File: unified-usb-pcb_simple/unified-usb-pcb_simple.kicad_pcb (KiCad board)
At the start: 2 copper layers, 30 x 34 mm, 12 parts, among them J1 USB_C_Receptacle_USB2.0, J2 USB_Out, U1 SRV05-4

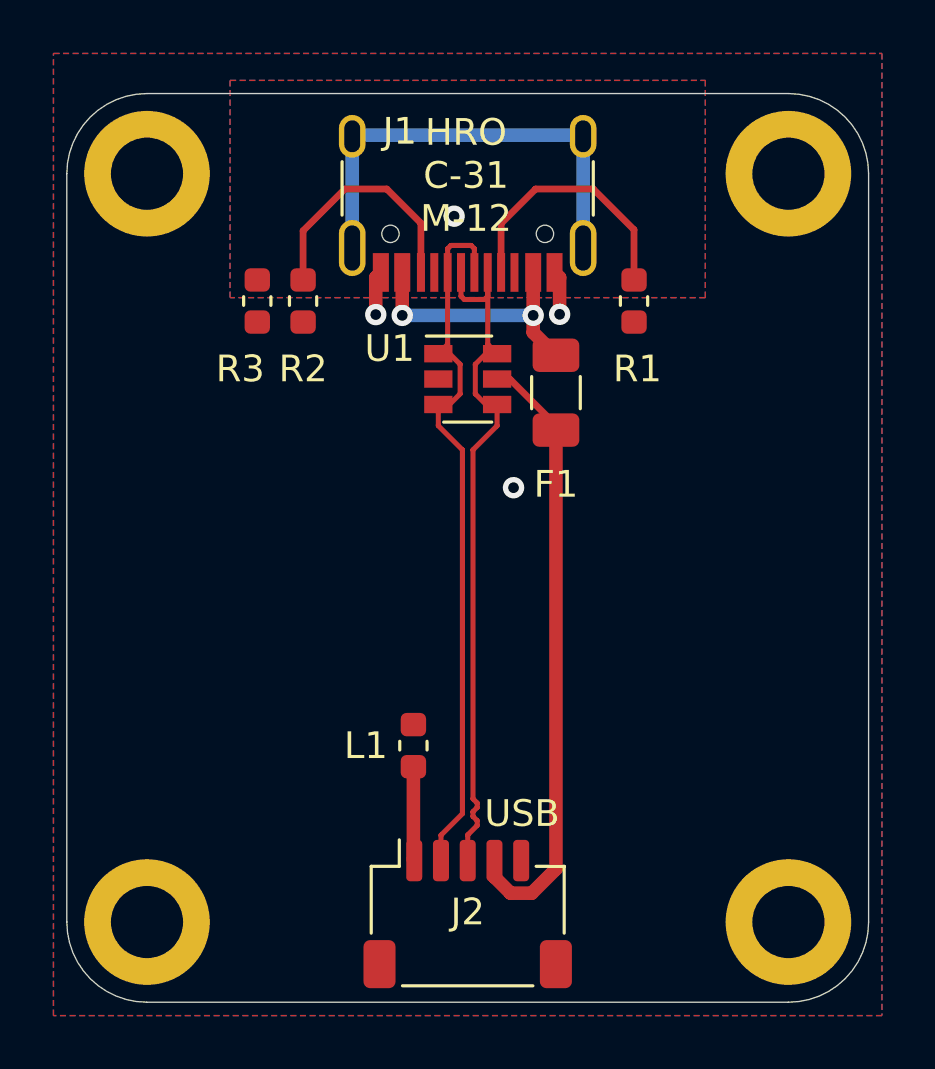
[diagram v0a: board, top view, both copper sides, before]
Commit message: slight rev bump - fixed battery pcb, re-exported new prod files for jlcpcb. Probably last commit, project no longer in active development
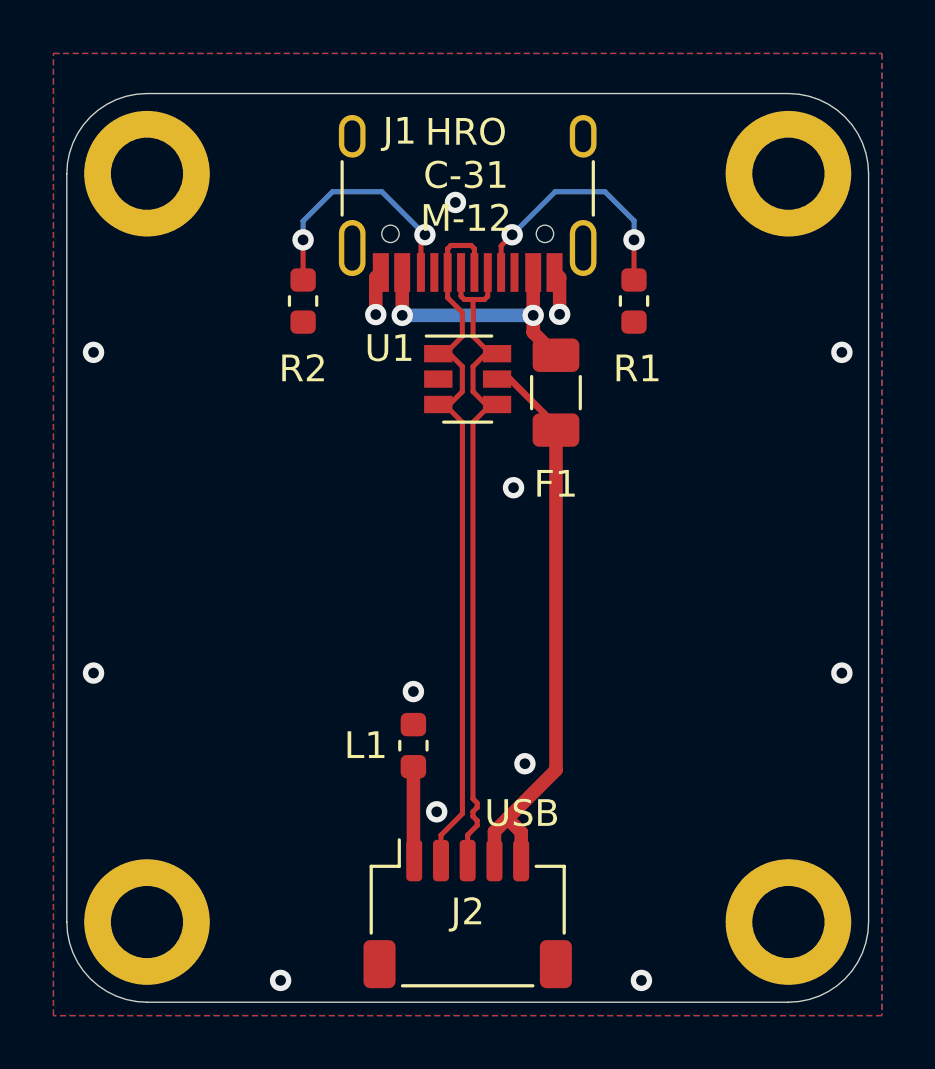
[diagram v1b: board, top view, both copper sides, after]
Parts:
- removed R3: 0, Resistor_SMD:R_0603_1608Metric
- R1, R2: value 5,1k -> 5.1k
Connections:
- H1 pad 1: GNDPWR -> Earth
- H2 pad 1: GNDPWR -> (no net)
- H3 pad 1: GNDPWR -> (no net)
- H4 pad 1: GNDPWR -> (no net)
- J1 pad A1: GNDPWR -> Earth
- J1 pad A12: GNDPWR -> Earth
- J1 pad A8: Net-(J1-PadA8) -> unconnected-(J1-PadA8)
- J1 pad B1: GNDPWR -> Earth
- J1 pad B12: GNDPWR -> Earth
- J1 pad B8: Net-(J1-PadB8) -> unconnected-(J1-PadB8)
- J2 pad 5: chgsense -> VOUT
- J2 pad MP: (no net) -> Earth
- L1 pad 2: GNDPWR -> Earth
- R1 pad 1: GNDPWR -> Earth
- R2 pad 1: GNDPWR -> Earth
- U1 pad 2: GNDPWR -> Earth
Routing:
- net Earth: track 17.0 -> 3.88 mm, vias 1 -> 13
- net GNDPWR: track 3.87 -> 0.00 mm, vias 3 -> 0
- net VOUT: track 23.1 -> 21.9 mm
- net USB_D+: track 26.9 -> 27.7 mm
- net Net-(J1-PadA5): track 9.85 -> 9.47 mm, vias 0 -> 2
- net Net-(J1-PadB5): track 9.23 -> 9.35 mm, vias 0 -> 2
- removed copper zone on B.Cu, net GNDPWR
- removed copper zone on F.Cu, net GNDPWR
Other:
- net class Default removed
- net class power removed
- board text added: "Type-C PCB [simple] rev 1.1 github.com/ebastler/unified-usb-pcb mpwr.xyz"
- board text removed: "Type-C PCB [simple] rev 1.0 github.com/ebastler/unified-usb-pcb mpwr.xyz"
